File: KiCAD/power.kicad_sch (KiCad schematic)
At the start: 64 parts, among them IC10 ADP7182ACPZN-R7, IC11 ADP150AUJZ-3.3-R7, IC4 ADP150AUJZ-3.3-R7, IC5 ADP150AUJZ-3.3-R7, IC6 ADP150AUJZ-3.3-R7, IC7 ADP150AUJZ-3.3-R7, IC8 LT1026CS8#PBF, IC9 ADP7118ARDZ

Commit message: REV 1.0.1 does not work. Updating BOM IDs.
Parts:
- C38, C39, C40, C41, C50, C51, C52, C53, C66, C73, C75: Mouser Part Number 80-C0805C104K8RAUTO -> 603-CC805KKX5R7BB475; Part Number C0805C104K8RACAUTO -> CC0805KKX5R7BB475
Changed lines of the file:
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@@
       (effects (font (size 1.27 1.27)) hide)
     )
-    (property "Part Number" "C0805C104K8RACAUTO" (id 4) (at 106.68 33.02 0)
-      (effects (font (size 1.27 1.27)) hide)
-    )
-    (property "Mouser Part Number" "80-C0805C104K8RAUTO" (id 5) (at 106.68 33.02 0)
+    (property "Part Number" "CC0805KKX5R7BB475" (id 4) (at 106.68 33.02 0)
+      (effects (font (size 1.27 1.27)) hide)
+    )
+    (property "Mouser Part Number" "603-CC805KKX5R7BB475" (id 5) (at 106.68 33.02 0)
       (effects (font (size 1.27 1.27)) hide)
     )
@@
       (effects (font (size 1.27 1.27)) hide)
     )
-    (property "Part Number" "C0805C104K8RACAUTO" (id 4) (at 153.67 124.46 0)
-      (effects (font (size 1.27 1.27)) hide)
-    )
-    (property "Mouser Part Number" "80-C0805C104K8RAUTO" (id 5) (at 153.67 124.46 0)
+    (property "Part Number" "CC0805KKX5R7BB475" (id 4) (at 153.67 124.46 0)
+      (effects (font (size 1.27 1.27)) hide)
+    )
+    (property "Mouser Part Number" "603-CC805KKX5R7BB475" (id 5) (at 153.67 124.46 0)
       (effects (font (size 1.27 1.27)) hide)
     )
@@
       (effects (font (size 1.27 1.27)) hide)
     )
-    (property "Part Number" "C0805C104K8RACAUTO" (id 4) (at 110.49 140.97 0)
-      (effects (font (size 1.27 1.27)) hide)
-    )
-    (property "Mouser Part Number" "80-C0805C104K8RAUTO" (id 5) (at 110.49 140.97 0)
+    (property "Part Number" "CC0805KKX5R7BB475" (id 4) (at 110.49 140.97 0)
+      (effects (font (size 1.27 1.27)) hide)
+    )
+    (property "Mouser Part Number" "603-CC805KKX5R7BB475" (id 5) (at 110.49 140.97 0)
       (effects (font (size 1.27 1.27)) hide)
     )
@@
       (effects (font (size 1.27 1.27)) hide)
     )
-    (property "Part Number" "C0805C104K8RACAUTO" (id 4) (at 33.02 31.75 0)
-      (effects (font (size 1.27 1.27)) hide)
-    )
-    (property "Mouser Part Number" "80-C0805C104K8RAUTO" (id 5) (at 33.02 31.75 0)
+    (property "Part Number" "CC0805KKX5R7BB475" (id 4) (at 33.02 31.75 0)
+      (effects (font (size 1.27 1.27)) hide)
+    )
+    (property "Mouser Part Number" "603-CC805KKX5R7BB475" (id 5) (at 33.02 31.75 0)
       (effects (font (size 1.27 1.27)) hide)
     )
@@
       (effects (font (size 1.27 1.27)) hide)
     )
-    (property "Part Number" "C0805C104K8RACAUTO" (id 4) (at 33.02 110.49 0)
-      (effects (font (size 1.27 1.27)) hide)
-    )
-    (property "Mouser Part Number" "80-C0805C104K8RAUTO" (id 5) (at 33.02 110.49 0)
+    (property "Part Number" "CC0805KKX5R7BB475" (id 4) (at 33.02 110.49 0)
+      (effects (font (size 1.27 1.27)) hide)
+    )
+    (property "Mouser Part Number" "603-CC805KKX5R7BB475" (id 5) (at 33.02 110.49 0)
       (effects (font (size 1.27 1.27)) hide)
     )
@@
       (effects (font (size 1.27 1.27)) hide)
     )
-    (property "Part Number" "C0805C104K8RACAUTO" (id 4) (at 33.02 170.18 0)
-      (effects (font (size 1.27 1.27)) hide)
-    )
-    (property "Mouser Part Number" "80-C0805C104K8RAUTO" (id 5) (at 33.02 170.18 0)
+    (property "Part Number" "CC0805KKX5R7BB475" (id 4) (at 33.02 170.18 0)
+      (effects (font (size 1.27 1.27)) hide)
+    )
+    (property "Mouser Part Number" "603-CC805KKX5R7BB475" (id 5) (at 33.02 170.18 0)
       (effects (font (size 1.27 1.27)) hide)
     )
@@
       (effects (font (size 1.27 1.27)) hide)
     )
-    (property "Part Number" "C0805C104K8RACAUTO" (id 4) (at 110.49 111.76 0)
-      (effects (font (size 1.27 1.27)) hide)
-    )
-    (property "Mouser Part Number" "80-C0805C104K8RAUTO" (id 5) (at 110.49 111.76 0)
+    (property "Part Number" "CC0805KKX5R7BB475" (id 4) (at 110.49 111.76 0)
+      (effects (font (size 1.27 1.27)) hide)
+    )
+    (property "Mouser Part Number" "603-CC805KKX5R7BB475" (id 5) (at 110.49 111.76 0)
       (effects (font (size 1.27 1.27)) hide)
     )
@@
       (effects (font (size 1.27 1.27)) hide)
     )
-    (property "Part Number" "C0805C104K8RACAUTO" (id 4) (at 110.49 171.45 0)
-      (effects (font (size 1.27 1.27)) hide)
-    )
-    (property "Mouser Part Number" "80-C0805C104K8RAUTO" (id 5) (at 110.49 171.45 0)
+    (property "Part Number" "CC0805KKX5R7BB475" (id 4) (at 110.49 171.45 0)
+      (effects (font (size 1.27 1.27)) hide)
+    )
+    (property "Mouser Part Number" "603-CC805KKX5R7BB475" (id 5) (at 110.49 171.45 0)
       (effects (font (size 1.27 1.27)) hide)
     )
@@
       (effects (font (size 1.27 1.27)) hide)
     )
-    (property "Part Number" "C0805C104K8RACAUTO" (id 4) (at 106.68 67.31 0)
-      (effects (font (size 1.27 1.27)) hide)
-    )
-    (property "Mouser Part Number" "80-C0805C104K8RAUTO" (id 5) (at 106.68 67.31 0)
+    (property "Part Number" "CC0805KKX5R7BB475" (id 4) (at 106.68 67.31 0)
+      (effects (font (size 1.27 1.27)) hide)
+    )
+    (property "Mouser Part Number" "603-CC805KKX5R7BB475" (id 5) (at 106.68 67.31 0)
       (effects (font (size 1.27 1.27)) hide)
     )
@@
       (effects (font (size 1.27 1.27)) hide)
     )
-    (property "Part Number" "C0805C104K8RACAUTO" (id 4) (at 33.02 66.04 0)
-      (effects (font (size 1.27 1.27)) hide)
-    )
-    (property "Mouser Part Number" "80-C0805C104K8RAUTO" (id 5) (at 33.02 66.04 0)
+    (property "Part Number" "CC0805KKX5R7BB475" (id 4) (at 33.02 66.04 0)
+      (effects (font (size 1.27 1.27)) hide)
+    )
+    (property "Mouser Part Number" "603-CC805KKX5R7BB475" (id 5) (at 33.02 66.04 0)
       (effects (font (size 1.27 1.27)) hide)
     )
@@
       (effects (font (size 1.27 1.27)) hide)
     )
-    (property "Part Number" "C0805C104K8RACAUTO" (id 4) (at 33.02 139.7 0)
-      (effects (font (size 1.27 1.27)) hide)
-    )
-    (property "Mouser Part Number" "80-C0805C104K8RAUTO" (id 5) (at 33.02 139.7 0)
-      (effects (font (size 1.27 1.27)) hide)
-    )
+    (property "Part Number" "CC0805KKX5R7BB475" (id 4) (at 33.02 139.7 0)
+      (effects (font (size 1.27 1.27)) hide)
+    )
+    (property "Mouser Part Number" "603-CC805KKX5R7BB475" (id 5) (at 33.02 139.7 0)
+      (effects (font (size 1.27 1.27)) hide)
+    )

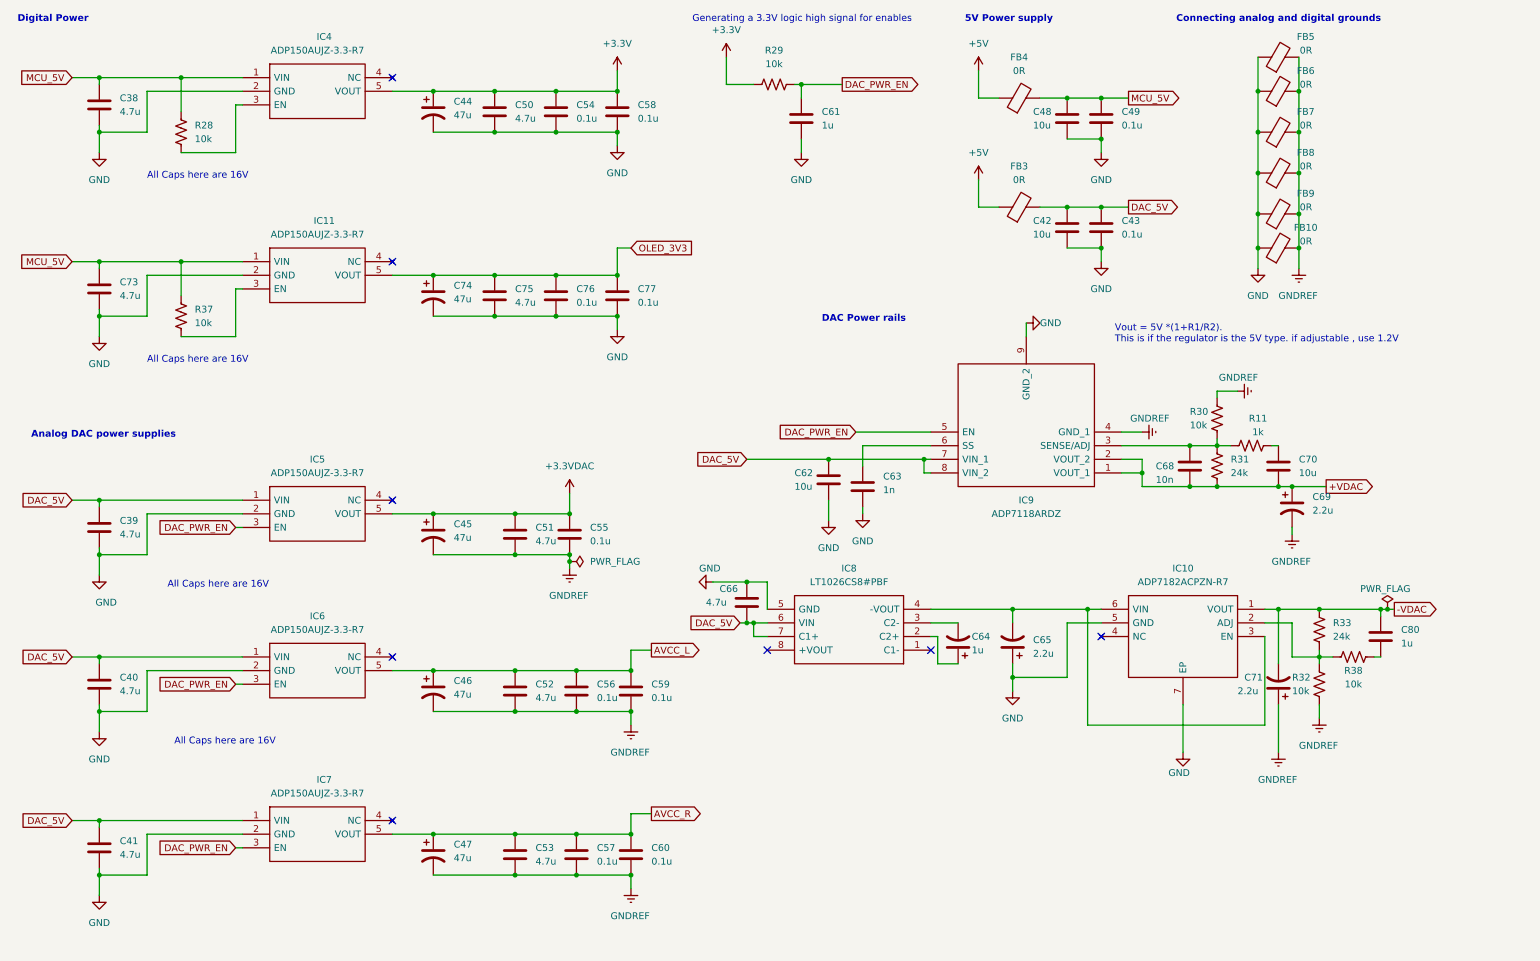
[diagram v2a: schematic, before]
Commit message: Fixing 3.3V being fed to VDDCORE. Swaping 3.3V LDOs to onsemi ones with higher output current
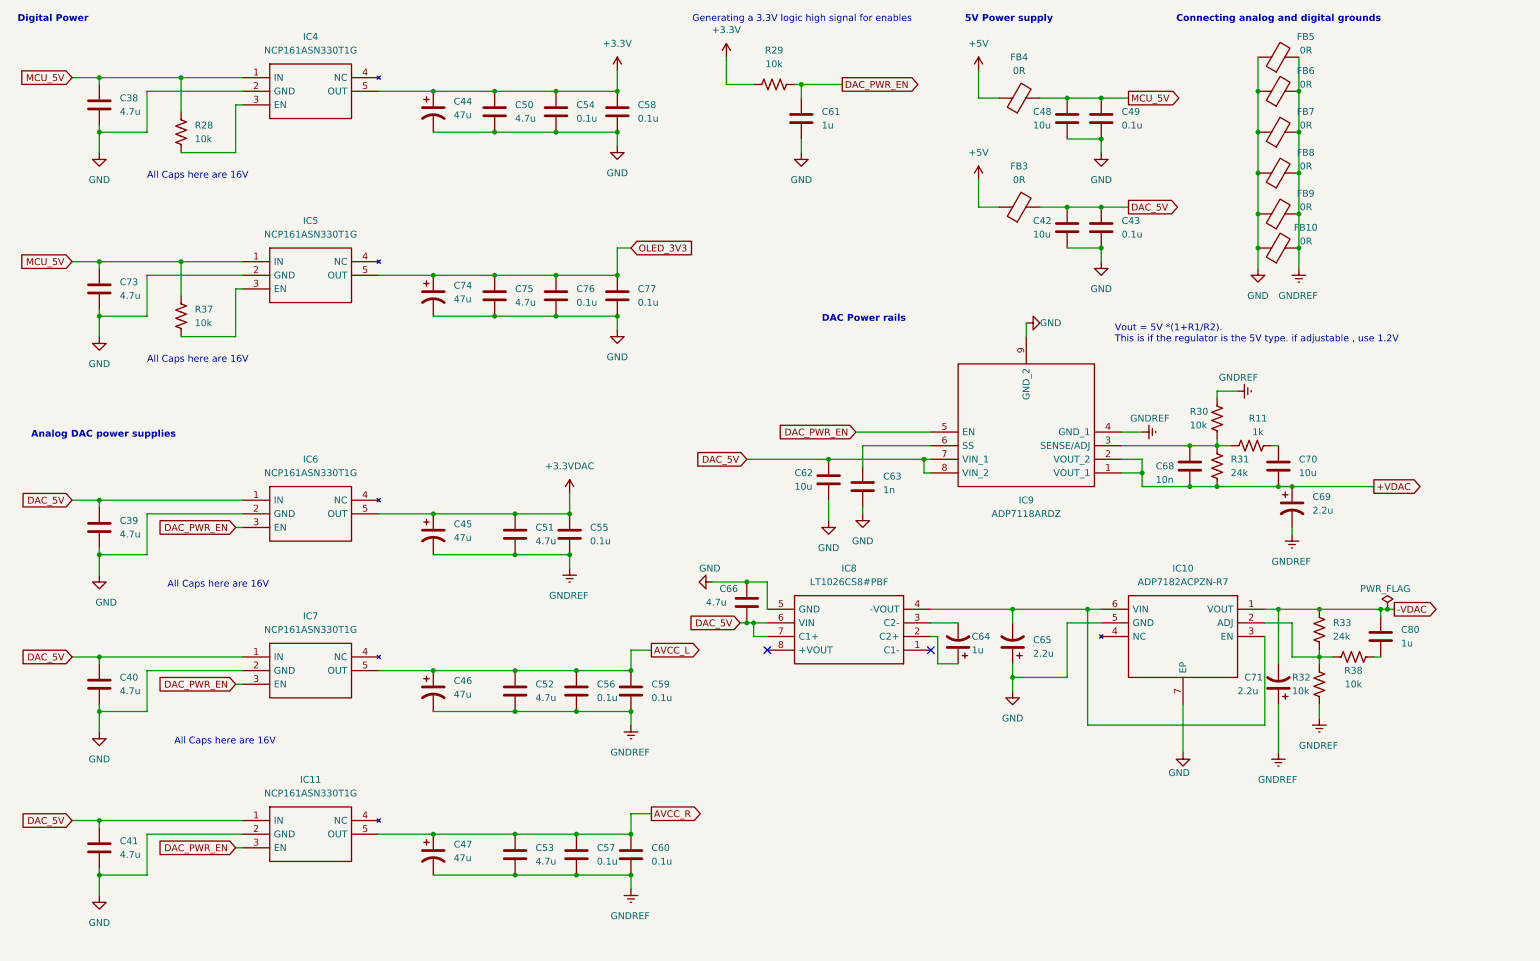
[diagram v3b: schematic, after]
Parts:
- removed IC11, IC4, IC5, IC6, IC7: ADP150AUJZ-3.3-R7, SamacSys_Parts:SOT95P280X100-5N, symbol SamacSys_Parts:ADP150AUJZ-3.3-R7
- added IC11, IC4, IC5, IC6, IC7: NCP161ASN330T1G, SOT95P280X145-5N, symbol SamacSys_Parts:NCP161ASN330T1G
- IC9: footprint SamacSys_Parts:SOIC127P600X175-9N -> SOIC127P600X175-9N
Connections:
- net +3.3VDAC: now also IC6.5 (OUT)
- net +3V3: now also IC4.5 (OUT)
- net AVCC_L: now also IC7.5 (OUT)
- net AVCC_R: now also IC11.5 (OUT)
- net DAC_5V: now also IC11.1 (IN), IC6.1 (IN), IC7.1 (IN)
- net DAC_PWR_EN: now also IC11.3 (EN), IC6.3 (EN), IC7.3 (EN)
- net GND: now also IC11.2 (GND), IC4.2 (GND), IC5.2 (GND), IC6.2 (GND), IC7.2 (GND)
- net MCU_5V: now also IC4.1 (IN), IC5.1 (IN)
- net OLED_3V3: now also IC5.5 (OUT)
- net at R28.1: now also IC4.3 (EN)
- net at R37.1: now also IC5.3 (EN)
- no-connect marks 8 -> 2

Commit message: Adding stuff for rev 2.0
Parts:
- removed C58, C77: 0.1u, Capacitor_SMD:C_0805_2012Metric_Pad1.18x1.45mm_HandSolder, symbol Device:C
- removed C64: 1u, Capacitor_THT:CP_Radial_D5.0mm_P2.00mm, symbol Device:C_Polarized_US
- removed C65: 2.2u, Capacitor_THT:CP_Radial_D4.0mm_P1.50mm, symbol Device:C_Polarized_US
- removed C70: 10u, Capacitor_SMD:C_0805_2012Metric_Pad1.18x1.45mm_HandSolder, symbol Device:C
- removed FB4: 0R, SamacSys_Parts:BEADC2012X110N, symbol Device:FerriteBead
- removed IC8: LT1026CS8#PBF, SamacSys_Parts:SOIC127P599X175-8N, symbol SamacSys_Parts:LT1026CS8#PBF
- removed IC9: ADP7118ARDZ, SOIC127P600X175-9N, symbol SamacSys_Parts:ADP7118ARDZ
- removed R31: 24k, Resistor_SMD:R_0805_2012Metric_Pad1.20x1.40mm_HandSolder, symbol Device:R_US
- added C64: 10u, Capacitor_SMD:C_0805_2012Metric_Pad1.18x1.45mm_HandSolder, symbol Device:C
- added C65: 4.7u, Capacitor_SMD:C_0805_2012Metric_Pad1.18x1.45mm_HandSolder, symbol Device:C
- added IC8: MAX889SESA+, SOIC127P600X175-8N, symbol SamacSys_Parts:MAX889SESA+
- added IC9: MAX38902AATA+T, SON50P200X200X80-9N-D, symbol SamacSys_Parts:MAX38902AATA+T
- added JP10, JP8, JP9: SolderJumper_2_Bridged, SolderJumper-2_P1.3mm_Bridged2Bar_Pad1.0x1.5mm, symbol Jumper:SolderJumper_2_Bridged
- added JP5, JP6, JP7: jumper, SolderJumper-2_P1.3mm_Bridged2Bar_Pad1.0x1.5mm, symbol Jumper:SolderJumper_2_Bridged
- C42, C48: Mouser Part Number 963-LMK212ABJ106KG8T -> 963-TMK212BBJ106KG-T; Part Number LMK212ABJ106KG8T -> TMK212BBJ106KG-T
- C62: value 10u -> 4.7u; Mouser Part Number 963-LMK212ABJ106KG8T -> 603-CC805KKX5R7BB475; Part Number LMK212ABJ106KG8T -> CC0805KKX5R7BB475
- C63: value 1n -> 2.2u; Mouser Part Number 581-0805YD102KAT2A -> 963-TMK212B7225KGHT; Part Number 0805YD102KAT2A -> TMK212B7225KGHT
- C66: value 4.7u -> 10u; Mouser Part Number 603-CC805KKX5R7BB475 -> 963-TMK212BBJ106KG-T; Part Number CC0805KKX5R7BB475 -> TMK212BBJ106KG-T
- C69: value 2.2u -> 47u; footprint Capacitor_THT:CP_Radial_D4.0mm_P1.50mm -> Capacitor_THT:CP_Radial_D5.0mm_P2.50mm; Mouser Part Number 667-ECE-A1HKA2R2 -> 667-ECA-1CHG470I; Part Number ECE-A1HKA2R2 -> ECA-1CHG470I
- R11: value 1k -> 100k; Mouser Part Number 667-ERA-6AEB102V -> 71-RCV0805100KJNEA; Part Number ERA-6AEB102V -> RCV0805100KJNEA
- R30: value 10k -> 100k; Mouser Part Number 603-RT0805BRD0710KL -> 71-RCV0805100KJNEA; Part Number RT0805BRD0710KL -> RCV0805100KJNEA
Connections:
- net MCU_5V is gone; now on net +5V: C38.1, C48.2, C49.1, C73.1, IC4.1 (IN), IC5.1 (IN), R28.2, R37.2
- net +VDAC: now also C68.1, C65.1, IC9.6 (OUTS), IC9.8 (OUT); no longer C68.2, C69.1
- net DAC_5V: now also C66.1, C69.1, R30.1, IC8.1 (IN), IC9.1 (IN), IC9.4 (SELA); no longer C66.2
- net DAC_PWR_EN: now also JP10.1 (A), JP5.2 (B), JP6.2 (B), JP7.2 (B), JP8.1 (A), JP9.1 (A); no longer IC11.3 (EN), IC6.3 (EN), IC7.3 (EN)
- net GND: now also C66.2, C69.2, C64.2, IC8.3 (GND), IC8.8 (AGND), IC9.2 (GND), IC9.9 (EP); no longer C63.2, C66.1
- net GNDREF: now also C65.2, IC9.5 (SELB); no longer C69.2, R30.2
- net at IC10.6 (VIN): now also R11.1, R30.2, C64.1, IC8.5 (OUT); no longer IC10.3 (EN)
- net at R11.2: now also IC8.7 (FB)
- net at C63.1: now also IC8.2 (CAP+)
- new net: IC6.3 (EN), JP7.1 (A)
- new net: C63.2, IC8.4 (CAP-)
- new net: IC8.6 (~{SHDN}), JP9.2 (B)
- new net: IC10.3 (EN), JP10.2 (B)
- new net: IC11.3 (EN), JP5.1 (A)
- new net: IC9.3 (EN), JP8.2 (B)
- new net: IC7.3 (EN), JP6.1 (A)
- new net: C68.2, IC9.7 (BYP)
- no-connect marks 2 -> 0
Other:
- note added: "For 4V output: (see datasheet for specifics) SELA = VIN SELB = GND"
- note added: "Use Low-ESR X7R Ceramic Caps for Voltage inverter"
- note removed: "Vout = 5V *(1+R1/R2). This is if the regulator is the 5V type. if adjustable , use 1.2V"
- moved on the sheet: C42, C43, C46, C52, C56, C59, C61, C62, C66, C68, R28, R29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
